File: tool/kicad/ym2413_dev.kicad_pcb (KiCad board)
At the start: 2 copper layers, 115 x 45 mm, 145 parts, among them J1 MICRO-USB-AB, K1 CONN_3, K2 CONN_3, P1 TEST_POINT, P10 TEST_POINT, P11 TEST_POINT, P12 TEST_POINT, P13 TEST_POINT, P14 TEST_POINT, P15 TEST_POINT, P16 TEST_POINT, P17 TEST_POINT, P18 TEST_POINT, P19 TEST_POINT, P2 TEST_POINT, P20 TEST_POINT, P21 TEST_POINT, P22 TEST_POINT, P23 TEST_POINT, P24 TEST_POINT, P25 TEST_POINT, P26 TEST_POINT, P27 TEST_POINT, P28 TEST_POINT, P29 TEST_POINT, P3 TEST_POINT, P30 CONN_3X2, P31 CONN_2, P32 CONN_2, P33 TEST_POINT, P34 TEST_POINT, P35 CONN_6, P37 TEST_POINT, P38 TEST_POINT, P4 TEST_POINT, P5 MIDI-IN, P6 TEST_POINT, P7 TEST_POINT, P8 TEST_POINT, P9 TEST_POINT, U1 SN74LVC2T45, U2 ST-USBLC6-2, U3 EFM32GG332, U4 YM2413, U5 LM386, U6 LM386, U7 ACPL-M21L, X1 48Mhz, X2 CRYSTAL

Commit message: work on 3V3 part
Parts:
- added C24: 4.7uF, 1206, F.Cu at (51.0, 79.5)
- moved D1 49.2 mm to (89.0, 62.5)
- moved R1 42.8 mm to (84.5, 62.5)
- moved C12 17.0 mm to (51.0, 77.0), turned to 0 degrees
- moved C17 11.8 mm to (41.9, 71.6), turned to 90 degrees
- moved R38 8.06 mm to (49.5, 71.0), turned to 180 degrees
- moved R46 4.69 mm to (118.2, 78.4)
- moved C15 4.65 mm to (80.5, 88.5)
- moved C16 4.60 mm to (80.8, 93.6)
- moved C18 4.50 mm to (115.7, 79.0)
- moved C19 4.50 mm to (115.7, 75.5)
- moved JP1 4.50 mm to (91.7, 96.0)
- moved JP2 4.50 mm to (99.2, 94.0)
- moved JP3 4.50 mm to (96.2, 94.0)
- moved JP4 4.50 mm to (91.7, 88.5)
- moved JP5 4.50 mm to (91.7, 91.5)
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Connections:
- net N-000003 renamed /SWCU
- net N-0000036 renamed /XTN
- net N-0000037 renamed /XTP
- net N-0000093 renamed /~RESETD
- C9 pad 2: N-00000100 (its old number) -> /DECOUPLE
- U3 pad 40: N-00000100 (its old number) -> /DECOUPLE
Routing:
- net GND: track 0.00 -> 34.8 mm, vias 0 -> 21
- net +3.3VADC: track 0.00 -> 16.2 mm
- net +5V: track 0.00 -> 15.4 mm
- net /VBUS_IN: track 0.00 -> 10.9 mm
- net +3.3V: track 0.00 -> 9.46 mm
- net /XTN: track 0.00 -> 8.47 mm
- net /D-: track 0.00 -> 7.71 mm
- net /D+: track 0.00 -> 7.71 mm
- net /GI_2: track 0.00 -> 5.78 mm
- net N-0000089: track 0.00 -> 5.77 mm
- net /XTP: track 0.00 -> 5.05 mm
- net /XIN3V3: track 0.00 -> 4.43 mm
- net /XOUT3V3: track 0.00 -> 4.23 mm
- net N-00000101: track 0.00 -> 3.81 mm
- net N-0000088: track 0.00 -> 3.77 mm
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- added copper zone on F.Cu, net +3.3V
- added copper zone on F.Cu, net /GI_2
- added copper zone on B.Cu, net GND
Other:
- net class Default: via_dia 0.889 -> 0.635; via_drill 0.635 -> 0.4318
- net class Power added: clearance 0.1524, trace_width 0.3048, via_dia 0.635, via_drill 0.4318
- rule trace_min: 0.254 -> 0.2032
- rule via_min_drill: 0.508 -> 0.4318
- rule via_min_size: 0.889 -> 0.635

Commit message: more layout work
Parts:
- moved R1 31.8 mm to (116.3, 64.2), turned to 180 degrees
- moved D1 31.2 mm to (120.2, 64.2), turned to 0 degrees
- moved P10 4.78 mm to (68.8, 92.0)
- moved D12 2.86 mm to (130.7, 72.4)
- moved U7 2.86 mm to (130.7, 78.4)
- moved R15 2.40 mm to (132.2, 69.3)
- moved P15 2.24 mm to (64.5, 93.5)
- moved P7 2.24 mm to (73.5, 93.5)
- moved P9 2.24 mm to (70.5, 93.5)
- moved P11 2.06 mm to (67.5, 93.5)
- moved P6 2.06 mm to (75.0, 92.0)
- moved P8 2.06 mm to (72.0, 92.0)
- moved R39 1.75 mm to (131.0, 103.1)
- moved C13 0.71 mm to (125.6, 99.3)
- moved C2 0.71 mm to (64.8, 89.6)
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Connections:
- net /MO/2 renamed /MOd2
- net /RO/2 renamed /ROd2
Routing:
- net +3.3V: track 9.46 -> 82.1 mm, vias 0 -> 4
- net +5V: track 15.4 -> 73.3 mm, vias 0 -> 4
- net /D0: track 0.00 -> 54.8 mm, vias 0 -> 2
- net /D1: track 0.00 -> 54.5 mm
- net /SWC: track 0.00 -> 53.5 mm, vias 0 -> 2
- net /~RESET: track 2.02 -> 50.5 mm, vias 0 -> 4
- net GND: track 34.8 -> 77.8 mm, vias 21 -> 43
- net /ROI: track 0.00 -> 41.1 mm
- net /D7: track 0.00 -> 40.8 mm, vias 0 -> 2
- net /SWD: track 0.00 -> 40.0 mm, vias 0 -> 3
- net /D6: track 0.00 -> 39.5 mm, vias 0 -> 2
- net /SWO: track 0.00 -> 37.3 mm, vias 0 -> 2
- net /XIN: track 2.10 -> 32.9 mm, vias 0 -> 2
- net /MOd2: track 0.00 -> 30.7 mm, vias 0 -> 2
- net /ROd2: track 0.00 -> 29.7 mm, vias 0 -> 2
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- added copper zone on F.Cu, net +5V
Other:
- net class Default: trace_width 0.254 -> 0.2032

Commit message: sync
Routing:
- net /~IC: track 0.00 -> 94.0 mm, vias 0 -> 2
- net /~CS: track 1.65 -> 89.1 mm, vias 0 -> 2
- net /~WE: track 1.67 -> 87.9 mm, vias 0 -> 2
- net /A0: track 1.65 -> 85.0 mm, vias 0 -> 2
- net /MIDI_IN: track 5.25 -> 88.4 mm, vias 0 -> 4
- net /MOd2: track 30.7 -> 86.7 mm, vias 2 -> 4
- net /ROd2: track 29.7 -> 75.9 mm, vias 2 -> 4

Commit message: route some of the LEDs
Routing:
- net /LED0: track 0.00 -> 34.8 mm, vias 0 -> 2
- net /LED4: track 0.00 -> 32.9 mm, vias 0 -> 2
- net /LED1: track 0.00 -> 32.7 mm, vias 0 -> 2
- net /LED3: track 0.00 -> 29.9 mm, vias 0 -> 2
- net /LED2: track 0.00 -> 29.7 mm, vias 0 -> 2
- net +3.3V: track 82.1 -> 98.8 mm, vias 4 -> 6
- net +5V: track 73.3 -> 84.5 mm, vias 4 -> 7

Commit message: finish first layout
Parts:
- removed D10, D11, D7, D8, D9: LED, 0805_LED
- removed R10, R13, R7, R8, R9: 3k3, 0603_S
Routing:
- net +3.3V: track 98.8 -> 141.4 mm, vias 6 -> 17
- net +5V: track 84.5 -> 106.0 mm
- net /GI_2: track 5.78 -> 23.4 mm
- net +3.3VADC: track 16.2 -> 22.5 mm
- net N-0000092: track 2.30 -> 0.00 mm
- net N-0000091 (its old number): track 2.30 -> 0.00 mm
- net N-0000078: track 2.30 -> 0.00 mm
- net N-0000074: track 2.30 -> 0.00 mm
- net N-0000072: track 2.30 -> 0.00 mm
- net GND: track 77.8 -> 76.6 mm, vias 43 -> 39
- net /ROd2: track 75.9 -> 76.8 mm

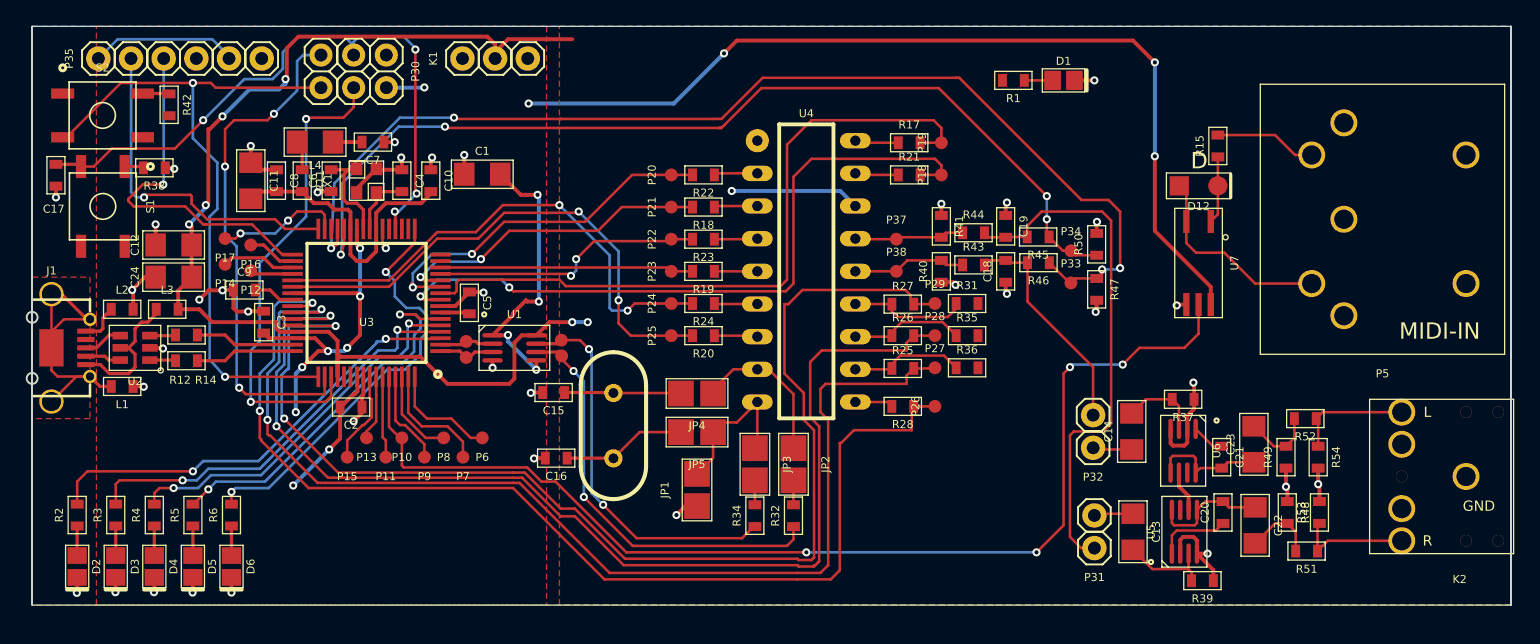
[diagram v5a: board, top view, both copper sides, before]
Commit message: re-add second 5 LEDs, but hook up to more reachable ports
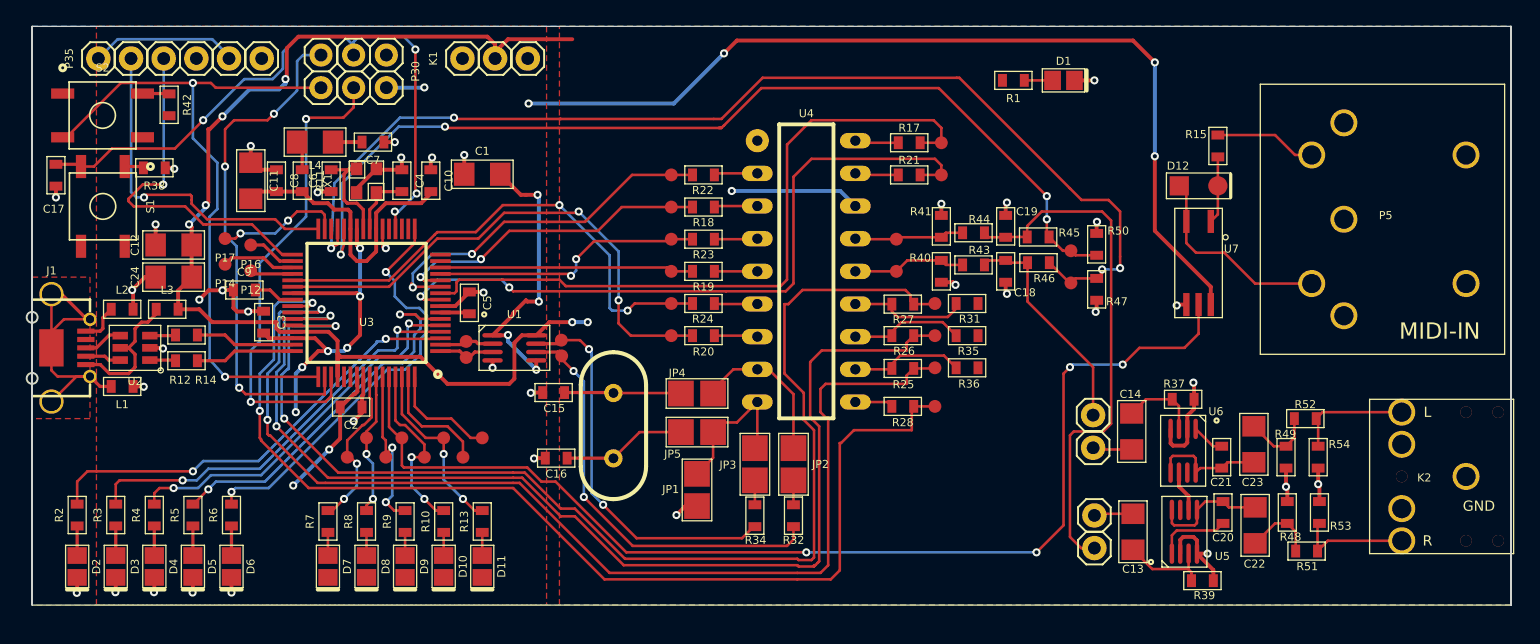
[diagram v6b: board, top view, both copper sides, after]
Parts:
- added D10: LED, 0805_LED, F.Cu at (72.0, 102.0)
- added D11: LED, 0805_LED, F.Cu at (75.0, 102.0)
- added D7: LED, 0805_LED, F.Cu at (63.0, 102.0)
- added D8: LED, 0805_LED, F.Cu at (66.0, 102.0)
- added D9: LED, 0805_LED, F.Cu at (69.0, 102.0)
- added R10: 3k3, 0603_S, F.Cu at (72.0, 98.5)
- added R13: 3k3, 0603_S, F.Cu at (75.0, 98.5)
- added R7: 3k3, 0603_S, F.Cu at (63.0, 98.5)
- added R8: 3k3, 0603_S, F.Cu at (66.0, 98.5)
- added R9: 3k3, 0603_S, F.Cu at (69.0, 98.5)
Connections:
- P11 pad 1: N-0000082 (its old number) -> /LED7
- P13 pad 1: N-0000081 (its old number) -> /LED6
- P15 pad 1: N-0000080 (its old number) -> /LED5
- P8 pad 1: N-0000084 -> /LED9
- P9 pad 1: N-0000083 -> /LED8
- U3 pad 15: /LED7 -> N-0000067
- U3 pad 16: /LED8 -> N-0000066
- U3 pad 18: /LED5 -> N-0000069
- U3 pad 19: /LED6 -> N-0000068
- U3 pad 21: /LED9 -> N-0000065
- U3 pad 57: N-0000080 (its old number) -> /LED5
- U3 pad 58: N-0000081 (its old number) -> /LED6
- U3 pad 59: N-0000082 (its old number) -> /LED7
- U3 pad 61: N-0000083 -> /LED8
- U3 pad 62: N-0000084 -> /LED9
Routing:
- net /LED9: track 0.00 -> 14.2 mm, vias 0 -> 2
- net /LED8: track 0.00 -> 14.0 mm, vias 0 -> 2
- net /LED7: track 0.00 -> 13.5 mm, vias 0 -> 2
- net /LED5: track 0.00 -> 12.9 mm, vias 0 -> 2
- net /LED6: track 0.00 -> 11.1 mm, vias 0 -> 2
- net N-0000083: track 7.42 -> 0.00 mm
- net N-0000080 (its old number): track 7.16 -> 0.00 mm
- net N-0000084: track 6.92 -> 0.00 mm
- net N-0000082 (its old number): track 6.35 -> 0.00 mm
- net N-0000081 (its old number): track 5.07 -> 0.00 mm
- net N-0000073: track 0.00 -> 1.80 mm
- net N-0000072: track 0.00 -> 1.80 mm
- net N-0000071: track 0.00 -> 1.80 mm
- net N-0000064: track 0.00 -> 1.80 mm
- net N-0000063: track 0.00 -> 1.80 mm

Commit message: wrap up silks
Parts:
- moved D10 0.50 mm to (72.0, 101.5)
- moved D11 0.50 mm to (75.0, 101.5)
- moved D2 0.50 mm to (43.5, 101.5)
- moved D3 0.50 mm to (46.5, 101.5)
- moved D4 0.50 mm to (49.5, 101.5)
- moved D5 0.50 mm to (52.5, 101.5)
- moved D6 0.50 mm to (55.5, 101.5)
- moved D7 0.50 mm to (63.0, 101.5)
- moved D8 0.50 mm to (66.0, 101.5)
- moved D9 0.50 mm to (69.0, 101.5)
- moved R10 0.25 mm to (72.0, 98.2)
- moved R13 0.25 mm to (75.0, 98.2)
- moved R7 0.25 mm to (63.0, 98.2)
- moved R8 0.25 mm to (66.0, 98.2)
- moved R9 0.25 mm to (69.0, 98.2)
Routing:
- net GND: track 76.6 -> 77.3 mm, vias 39 -> 44
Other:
- outline, holes or cut-outs redrawn
- board text added: "openMSX"
- board text added: "v0"
- board text added: "ym2413"

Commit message: cleanup
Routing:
- net +5V: track 106.0 -> 97.3 mm, vias 7 -> 8
- net +3.3V: track 141.4 -> 133.4 mm, vias 17 -> 15
- net /MOd2: vias 4 -> 6
- net /ROd2: vias 4 -> 6
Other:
- board text added: "0aa6025eaf4fbd4d714dfac16376bee86e5f8e5e"
